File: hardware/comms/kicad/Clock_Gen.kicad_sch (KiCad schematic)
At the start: 13 parts, among them Y1 Crystal_GND2, Y2 Si5351A-B-GT

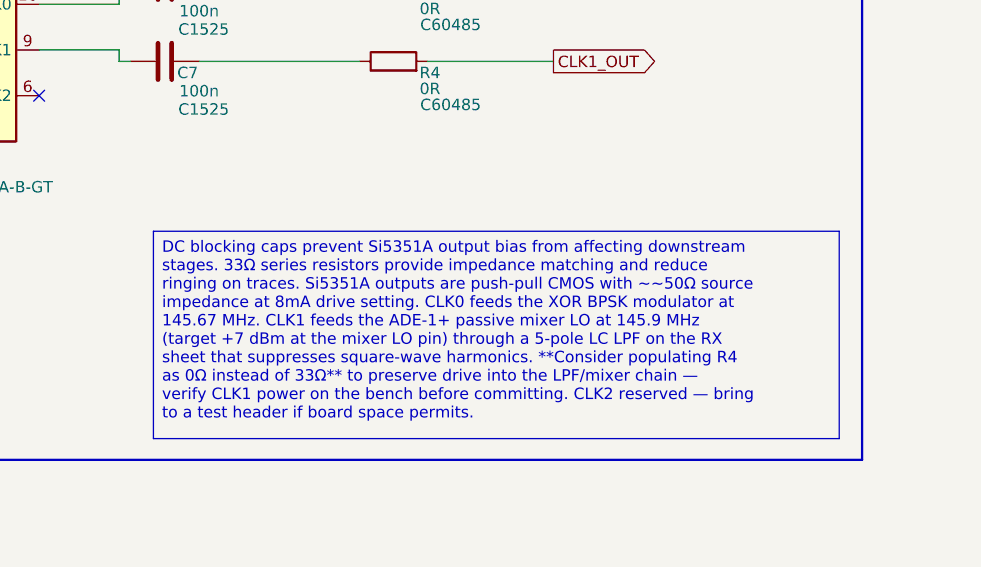
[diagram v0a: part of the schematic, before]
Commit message: comms/kicad: rename project and sheets, correct schematic text
  Renames
  - transciever_kicad.{pro,sch,pcb} -> transceiver.{pro,sch,pcb}: the
    project name was misspelled, and the _kicad suffix was redundant
    inside a kicad/ directory.
  - Sheet files lose their spaces: Clock_Gen, Digital_Control, RX_Chain,
    TX_Chain. Sheetname keeps its space -- that is the label drawn on the
    sheet, not a path.
  - References updated in four places, not one: 4 Sheetfile properties in
    the root schematic, 186 per-symbol (project ...) instances across every
    sheet, 68 per-footprint (sheetfile ...) entries in the PCB, and
    meta.filename plus the root sheet name in the project file. Verified
    afterwards that all sheet references resolve, no sheet is orphaned, and
    the project file still parses.

  Spelling and stale labels
  - Title block: Revsion -> Revision, Repsoitory -> Repository, repository
    path centisat -> ember, project named EMBER.
  - PCI-104 -> CSKB in three files. PCI-104 is a different real standard,
    and the same sheet's own revision history records the bus being renamed
    to CSKB back at rev 0.4.
  - Status LED's -> Status LEDs; +20 db -> +20 dB; RX SMA < - -> <-.
  - The tripler note named BRF92A as the flight transistor: misspelled, and
    superseded by the 2SC3356 actually placed. Corrected to 2SC3356 with
    the MMBT3904-footprint note the implementation plan records. The
    ft=5 GHz figure is dropped rather than reassigned to a part it was not
    measured against.
  - Power sheet: the D4 forward-drop note referred to the SA612, replaced
    by the ADE-1+ back at rev 0.5. Now names the PSA4-5043+.
 Altium-to-KiCad text damage
  Three separate corruptions, classified before replacing so that real
  values were not caught up in it -- ~21 dB and ~20 dB both contain a
  literal ~2 and would have been mangled by a blind pass.
  - 144 table column separators rendered as literal ~2; now |, so the
    sheet index, rail summary, net c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
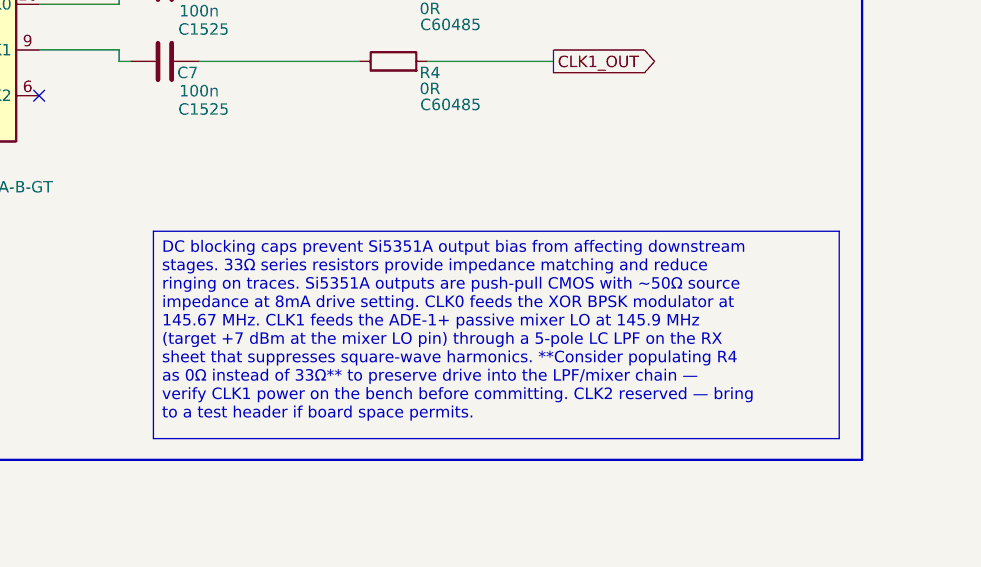
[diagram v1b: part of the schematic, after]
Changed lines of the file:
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@@
 		)
 	)
-	(text_box "DC blocking caps prevent Si5351A output bias from affecting downstream stages. 33Ω series resistors provide impedance matching and reduce ringing on traces. Si5351A outputs are push-pull CMOS with ~~50Ω source impedance at 8mA drive setting. CLK0 feeds the XOR BPSK modulator at 145.67 MHz. CLK1 feeds the ADE-1+ passive mixer LO at 145.9 MHz (target +7 dBm at the mixer LO pin) through a 5-pole LC LPF on the RX sheet that suppresses square-wave harmonics. **Consider populating R4 as 0Ω instead of 33Ω** to preserve drive into the LPF/mixer chain — verify CLK1 power on the bench before committing. CLK2 reserved — bring to a test header if board space permits."
+	(text_box "DC blocking caps prevent Si5351A output bias from affecting downstream stages. 33Ω series resistors provide impedance matching and reduce ringing on traces. Si5351A outputs are push-pull CMOS with ~50Ω source impedance at 8mA drive setting. CLK0 feeds the XOR BPSK modulator at 145.67 MHz. CLK1 feeds the ADE-1+ passive mixer LO at 145.9 MHz (target +7 dBm at the mixer LO pin) through a 5-pole LC LPF on the RX sheet that suppresses square-wave harmonics. **Consider populating R4 as 0Ω instead of 33Ω** to preserve drive into the LPF/mixer chain — verify CLK1 power on the bench before committing. CLK2 reserved — bring to a test header if board space permits."
 		(exclude_from_sim no)
 		(at 161.29 138.2522 0)
@@
 		)
 		(instances
-			(project "transciever_kicad"
+			(project "transceiver"
 				(path "/c034ea61-6551-4f92-af2a-65337e5cc22a/f9c62eb1-d7c0-4e60-a61d-f835f0c0a42e"
 					(reference "R1")
@@
 		)
 		(instances
-			(project "transciever_kicad"
+			(project "transceiver"
 				(path "/c034ea61-6551-4f92-af2a-65337e5cc22a/f9c62eb1-d7c0-4e60-a61d-f835f0c0a42e"
 					(reference "R3")
@@
 		)
 		(instances
-			(project "transciever_kicad"
+			(project "transceiver"
 				(path "/c034ea61-6551-4f92-af2a-65337e5cc22a/f9c62eb1-d7c0-4e60-a61d-f835f0c0a42e"
 					(reference "#PWR07")
@@
 		)
 		(instances
-			(project "transciever_kicad"
+			(project "transceiver"
 				(path "/c034ea61-6551-4f92-af2a-65337e5cc22a/f9c62eb1-d7c0-4e60-a61d-f835f0c0a42e"
 					(reference "C4")
@@
 		)
 		(instances
-			(project "transciever_kicad"
+			(project "transceiver"
 				(path "/c034ea61-6551-4f92-af2a-65337e5cc22a/f9c62eb1-d7c0-4e60-a61d-f835f0c0a42e"
 					(reference "#PWR08")
@@
 		)
 		(instances
-			(project "transciever_kicad"
+			(project "transceiver"
 				(path "/c034ea61-6551-4f92-af2a-65337e5cc22a/f9c62eb1-d7c0-4e60-a61d-f835f0c0a42e"
 					(reference "#PWR06")
@@
 		)
 		(instances
-			(project "transciever_kicad"
+			(project "transceiver"
 				(path "/c034ea61-6551-4f92-af2a-65337e5cc22a/f9c62eb1-d7c0-4e60-a61d-f835f0c0a42e"
 					(reference "C5")
@@
 		)
 		(instances
-			(project "transciever_kicad"
+			(project "transceiver"
 				(path "/c034ea61-6551-4f92-af2a-65337e5cc22a/f9c62eb1-d7c0-4e60-a61d-f835f0c0a42e"
 					(reference "#PWR011")
@@
 		)
 		(instances
-			(project "transciever_kicad"
+			(project "transceiver"
 				(path "/c034ea61-6551-4f92-af2a-65337e5cc22a/f9c62eb1-d7c0-4e60-a61d-f835f0c0a42e"
 					(reference "R4")
@@
 		)
 		(instances
-			(project "transciever_kicad"
+			(project "transceiver"
 				(path "/c034ea61-6551-4f92-af2a-65337e5cc22a/f9c62eb1-d7c0-4e60-a61d-f835f0c0a42e"
 					(reference "#PWR012")
@@
 		)
 		(instances
-			(project "transciever_kicad"
+			(project "transceiver"
 				(path "/c034ea61-6551-4f92-af2a-65337e5cc22a/f9c62eb1-d7c0-4e60-a61d-f835f0c0a42e"
 					(reference "R2")
@@
 		)
 		(instances
-			(project "transciever_kicad"
+			(project "transceiver"
 				(path "/c034ea61-6551-4f92-af2a-65337e5cc22a/f9c62eb1-d7c0-4e60-a61d-f835f0c0a42e"
 					(reference "#PWR01")
@@
 		)
 		(instances
-			(project "transciever_kicad"
+			(project "transceiver"
 				(path "/c034ea61-6551-4f92-af2a-65337e5cc22a/f9c62eb1-d7c0-4e60-a61d-f835f0c0a42e"
 					(reference "Y2")
@@
 		)
 		(instances
-			(project "transciever_kicad"
+			(project "transceiver"
 				(path "/c034ea61-6551-4f92-af2a-65337e5cc22a/f9c62eb1-d7c0-4e60-a61d-f835f0c0a42e"
 					(reference "#PWR02")
@@
 		)
 		(instances
-			(project "transciever_kicad"
+			(project "transceiver"
 				(path "/c034ea61-6551-4f92-af2a-65337e5cc22a/f9c62eb1-d7c0-4e60-a61d-f835f0c0a42e"
 					(reference "#PWR09")
@@
 		)
 		(instances
-			(project "transciever_kicad"
+			(project "transceiver"
 				(path "/c034ea61-6551-4f92-af2a-65337e5cc22a/f9c62eb1-d7c0-4e60-a61d-f835f0c0a42e"
 					(reference "C6")
@@
 		)
 		(instances
-			(project "transciever_kicad"
+			(project "transceiver"
 				(path "/c034ea61-6551-4f92-af2a-65337e5cc22a/f9c62eb1-d7c0-4e60-a61d-f835f0c0a42e"
 					(reference "Y1")
@@
 		)
 		(instances
-			(project "transciever_kicad"
+			(project "transceiver"
 				(path "/c034ea61-6551-4f92-af2a-65337e5cc22a/f9c62eb1-d7c0-4e60-a61d-f835f0c0a42e"
 					(reference "C3")
@@
 		)
 		(instances
-			(project "transciever_kicad"
+			(project "transceiver"
 				(path "/c034ea61-6551-4f92-af2a-65337e5cc22a/f9c62eb1-d7c0-4e60-a61d-f835f0c0a42e"
 					(reference "C2")
@@
 		)
 		(instances
-			(project "transciever_kicad"
+			(project "transceiver"
 				(path "/c034ea61-6551-4f92-af2a-65337e5cc22a/f9c62eb1-d7c0-4e60-a61d-f835f0c0a42e"
 					(reference "#PWR04")
@@
 		)
 		(instances
-			(project "transciever_kicad"
+			(project "transceiver"
 				(path "/c034ea61-6551-4f92-af2a-65337e5cc22a/f9c62eb1-d7c0-4e60-a61d-f835f0c0a42e"
 					(reference "#PWR03")
@@
 		)
 		(instances
-			(project "transciever_kicad"
+			(project "transceiver"
 				(path "/c034ea61-6551-4f92-af2a-65337e5cc22a/f9c62eb1-d7c0-4e60-a61d-f835f0c0a42e"
 					(reference "C1")
@@
 		)
 		(instances
-			(project "transciever_kicad"
+			(project "transceiver"
 				(path "/c034ea61-6551-4f92-af2a-65337e5cc22a/f9c62eb1-d7c0-4e60-a61d-f835f0c0a42e"
 					(reference "C7")

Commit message: Repair UHF/UHF comms schematic and document PCB blockers
Correct PSA4 LNA and Hottech transistor pin mappings, RX capacitor values, and BPSK net labeling.

Assign verified XOR, resistor, and test-point footprints. Correct bulk capacitor polarity and add Panasonic land patterns.

Add project RF libraries, pin-map audit, and TOOD checklist. Record unresolved library loading, connectivity export, and PCB synchronization issues.
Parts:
- R3, R4: footprint (none) -> Resistor_SMD:R_0402_1005Metric; Manufacturer (none) -> YAGEO; Manufacturer Part # (none) -> RC0402JR-070RL
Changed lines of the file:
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@@
 		(title "CubeSat Comms -- Clock Generator")
 		(rev "A")
+		(comment 9 "UHF/UHF revision in review - not for fabrication")
 	)
 	(rectangle
@@
 			)
 		)
-		(property "Footprint" ""
+		(property "Footprint" "Resistor_SMD:R_0402_1005Metric"
 			(at 187.96 112.268 90)
 			(hide yes)
@@
 			)
 		)
-		(property "Manufacturer Part #" ""
+		(property "Manufacturer Part #" "RC0402JR-070RL"
 			(at 187.96 110.49 90)
 			(hide yes)
@@
 		(property "LCSC Part #" "C60485"
 			(at 194.31 115.316 90)
+			(show_name no)
+			(do_not_autoplace no)
+			(effects
+				(font
+					(size 1.27 1.27)
+				)
+			)
+		)
+		(property "Manufacturer" "YAGEO"
+			(at 187.96 110.49 0)
+			(hide yes)
 			(show_name no)
 			(do_not_autoplace no)
@@
 			)
 		)
-		(property "Footprint" ""
+		(property "Footprint" "Resistor_SMD:R_0402_1005Metric"
 			(at 187.96 121.158 90)
 			(hide yes)
@@
 			)
 		)
-		(property "Manufacturer Part #" ""
+		(property "Manufacturer Part #" "RC0402JR-070RL"
 			(at 187.96 119.38 90)
 			(hide yes)
@@
 			(show_name no)
 			(do_not_autoplace no)
+			(effects
+				(font
+					(size 1.27 1.27)
+				)
+			)
+		)
+		(property "Manufacturer" "YAGEO"
+			(at 187.96 119.38 0)
+			(hide yes)
+			(show_name no)
+			(do_not_autoplace no)
